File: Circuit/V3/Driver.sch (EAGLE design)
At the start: 36 parts

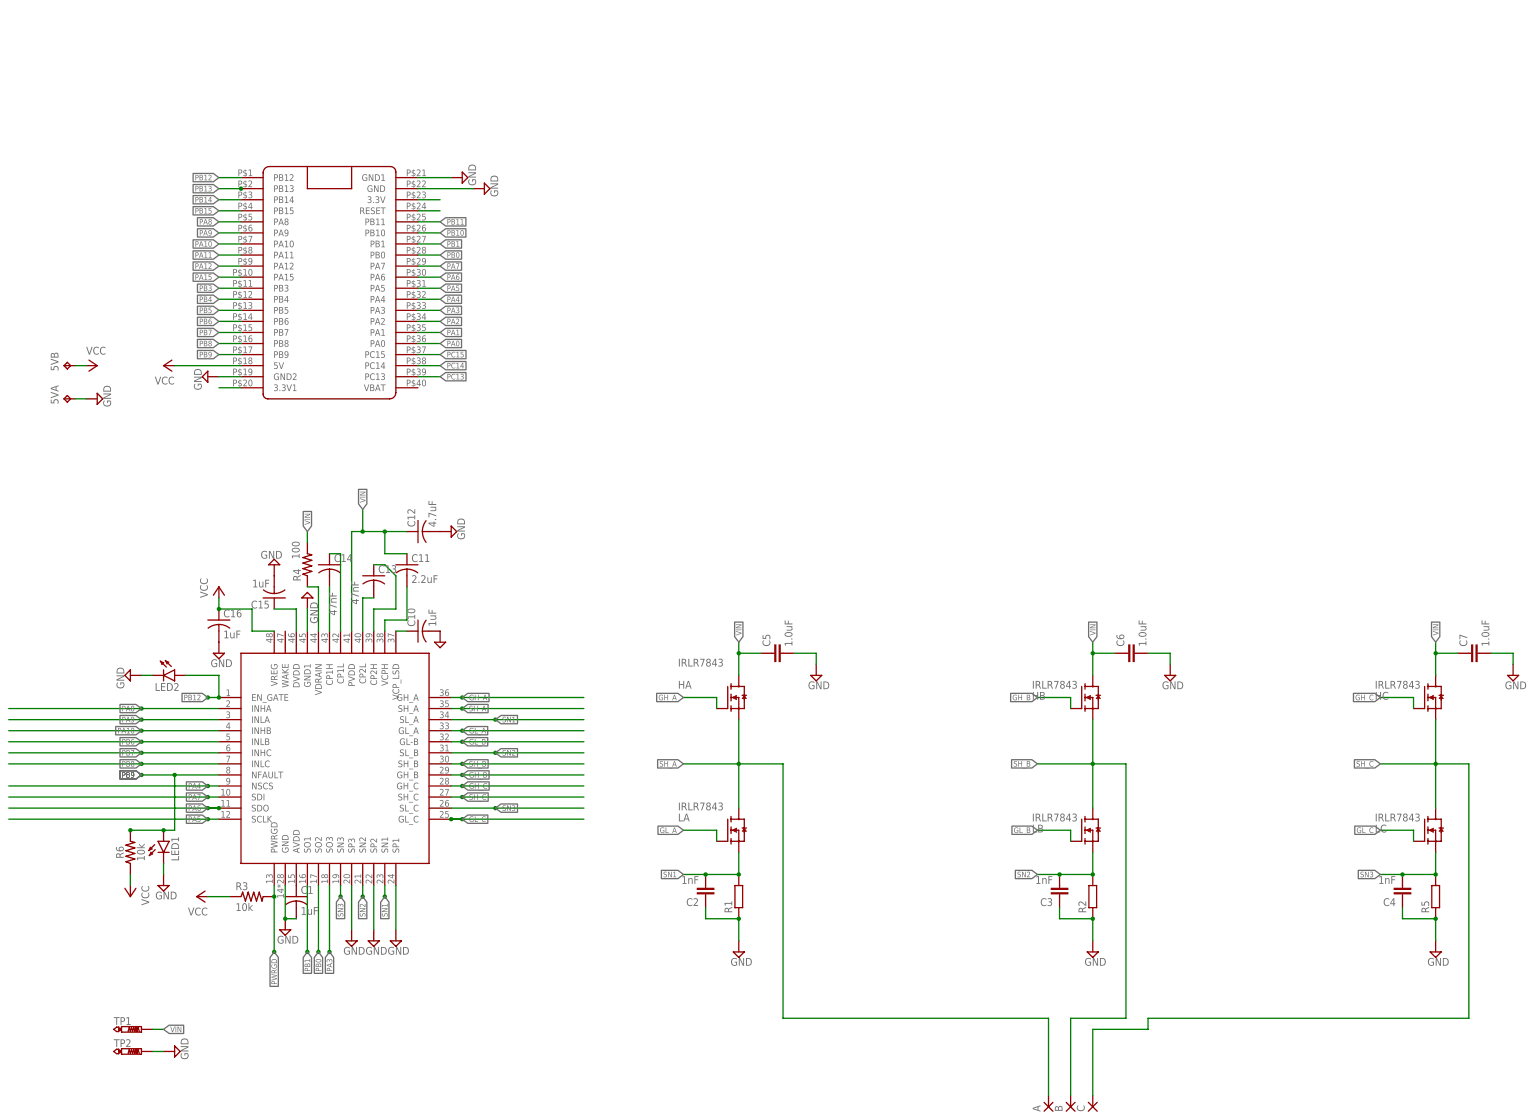
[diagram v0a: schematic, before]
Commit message: Change the orginal motor gate driver(DRV8305) to DRV8303 in schematic
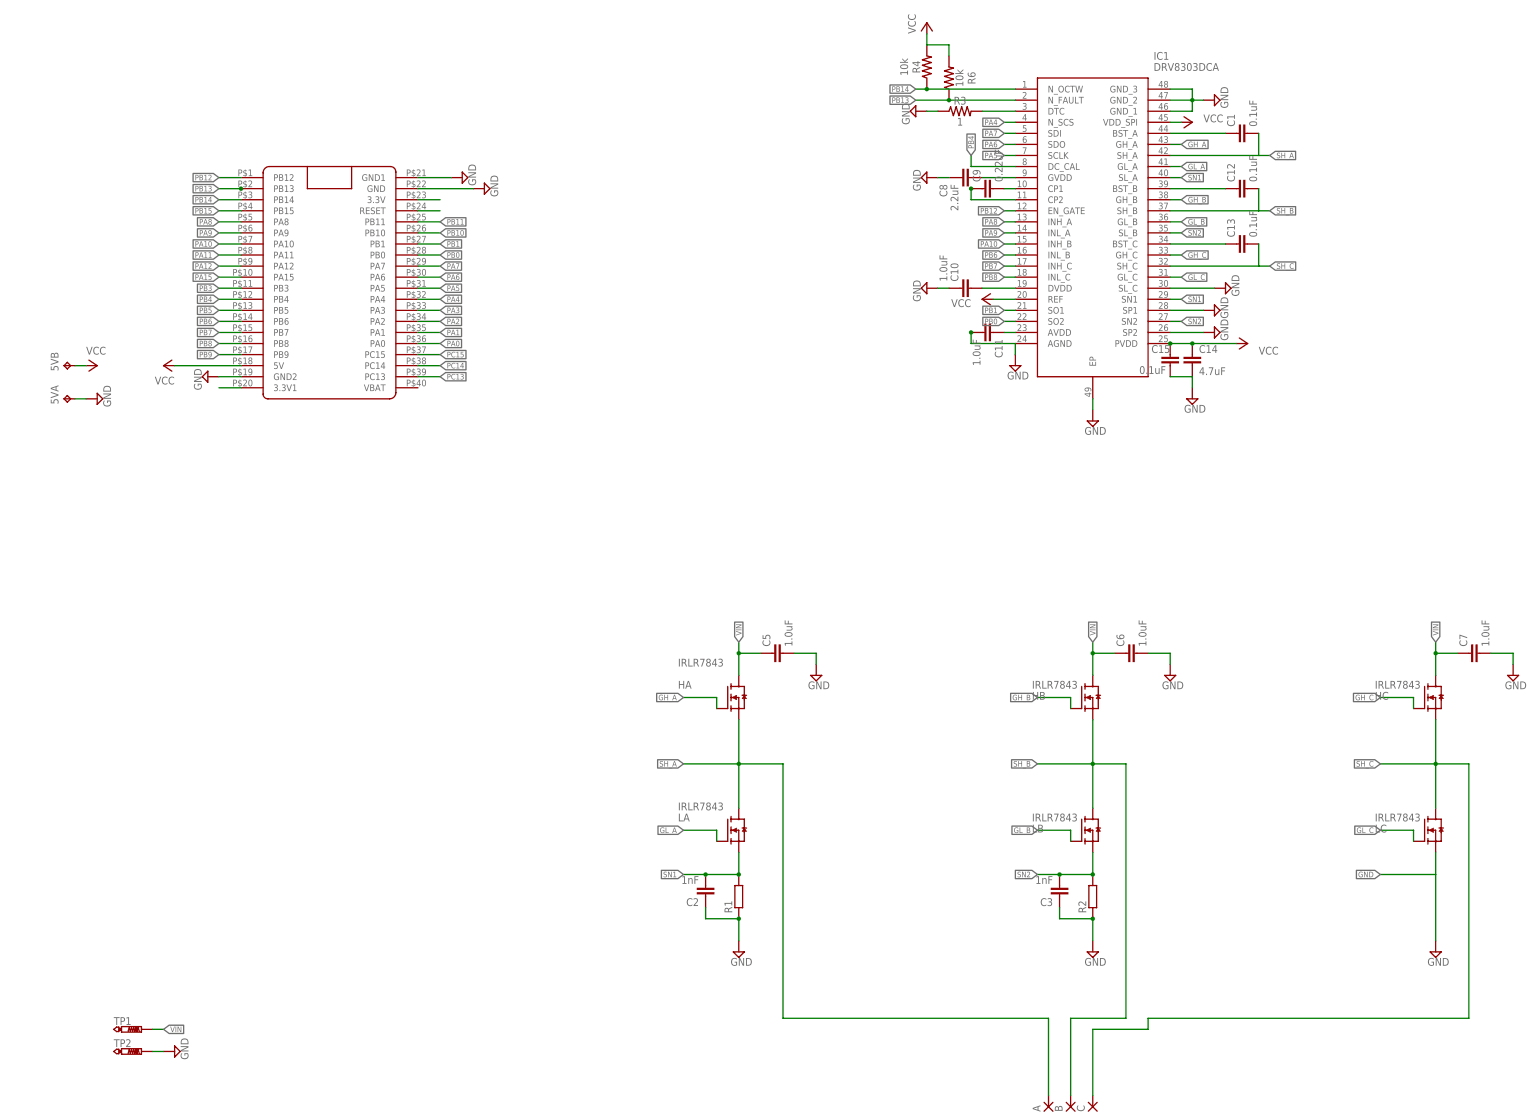
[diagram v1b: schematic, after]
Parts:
- removed C16: 1uF, rcl:C-USC0603
- removed C4: 1nF, SparkFun-Capacitors:1.0NF/1000PF-0603-50V-10%
- removed LED1, LED2: (no value), led:LEDCHIPLED_0805
- removed R5: (no value), rcl:R-EU_R2512
- removed U$3: DRV8305, BLDC project:DRV8305
- added C8: 2.2uF, SparkFun-Capacitors:2.2UF-0603-10V-20%
- added C9: 0.22uF, SparkFun-Capacitors:0.22UF-0603-25V-10%
- added IC1: DRV8303DCA, DRV8303DCA:DRV8303DCA
- C1, C15: value 1uF -> 0.1uF; device rcl:C-USC0603 -> SparkFun-Capacitors:0.1UF-0603-25V-(+80/-20%)
- C10: value 1uF -> 1.0uF; device rcl:C-USC0603 -> SparkFun-Capacitors:1.0UF-0603-16V-10%
- C11: value 2.2uF -> 1.0uF; device rcl:C-USC0603 -> SparkFun-Capacitors:1.0UF-0603-16V-10%
- C12: value 4.7uF -> 0.1uF; device rcl:C-USC0603 -> SparkFun-Capacitors:0.1UF-0603-25V-(+80/-20%)
- C13: value 47nF -> 0.1uF; device rcl:C-USC0603 -> SparkFun-Capacitors:0.1UF-0603-25V-(+80/-20%)
- C14: value 47nF -> 4.7uF; device rcl:C-USC0603 -> SparkFun-Capacitors:4.7UF-0603-35V-(20%)
- R3: value 10k -> 1; device rcl:R-US_R0603 -> SparkFun-Resistors:1OHM-0603-1/10W-1%
- R4: value 100 -> 10k; device rcl:R-US_R0603 -> SparkFun-Resistors:10KOHM-0603-1/10W-1%
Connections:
- removed net CP1H: C14.2, U$3.CP1H
- removed net CP1L: C14.1, U$3.CP1L
- removed net CP2H: C13.1, U$3.CP2H
- removed net CP2L: C13.2, U$3.CP2L
- removed net DVDD: C15.1, U$3.DVDD
- removed net N$15: C1.1, U$3.AVDD
- removed net PWRGD: R3.2, U$3.PWRGD
- removed net SN3: C4.2, LC.S, R5.2, U$3.SL_C, U$3.SN3
- removed net VCPH: C11.2, U$3.VCPH
- removed net VCP_LSD: C10.1, U$3.VCP_LSD
- removed net VDRAIN: R4.1, U$3.VDRAIN
- new net N$14: C13.1, IC1.BST_C
- new net N$2: C1.1, IC1.BST_A
- new net N$26: IC1.DTC, R3.2
- new net N$32: C8.1, IC1.GVDD
- new net N$33: C9.2, IC1.CP1
- new net N$34: C9.1, IC1.CP2
- new net N$43: C10.2, IC1.DVDD
- new net N$47: C11.1, IC1.AVDD
- new net N$9: C12.1, IC1.BST_B
- net GH_A: now also IC1.GH_A; no longer U$3.GH_A
- net GH_B: now also IC1.GH_B; no longer U$3.GH_B
- net GH_C: now also IC1.GH_C; no longer U$3.GH_C
- net GL_A: now also IC1.GL_A; no longer U$3.GL_A
- net GL_B: now also IC1.GL_B; no longer U$3.GL-B
- net GL_C: now also IC1.GL_C; no longer U$3.GL_C
- net GND: now also C10.1, C11.2, C14.2, C8.2, IC1.AGND, IC1.EP, IC1.GND_1, IC1.GND_2, IC1.GND_3, IC1.SL_C, IC1.SP1, IC1.SP2, LC.S, R3.1; no longer C1.2, C10.2, C12.2, C16.2, C4.1, LED1.C, LED2.C, R5.1, U$3.GND, U$3.GND1, U$3.SP1, U$3.SP2, U$3.SP3
- net PA10: now also IC1.INH_B; no longer U$3.INHB
- net PA3: no longer U$3.SO3
- net PA4: now also IC1.N_SCS; no longer U$3.NSCS
- net PA5: now also IC1.SCLK; no longer U$3.SCLK
- net PA6: now also IC1.SDO; no longer U$3.SDO
- net PA7: now also IC1.SDI; no longer U$3.SDI
- net PA8: now also IC1.INH_A; no longer U$3.INHA
- net PA9: now also IC1.INL_A; no longer U$3.INLA
- net PB0: now also IC1.SO2; no longer U$3.SO2
- net PB1: now also IC1.SO1; no longer U$3.SO1
- net PB12: now also IC1.EN_GATE; no longer LED2.A, U$3.EN_GATE
- net PB13: now also IC1.N_FAULT, R6.1
- net PB14: now also IC1.N_OCTW, R4.1
- net PB4: now also IC1.DC_CAL
- net PB6: now also IC1.INL_B; no longer U$3.INLB
- net PB7: now also IC1.INH_C; no longer U$3.INHC
- net PB8: now also IC1.INL_C; no longer U$3.INLC
- net PB9: no longer LED1.A, R6.2, U$3.NFAULT
- net SH_A: now also C1.2, IC1.SH_A; no longer U$3.SH_A
- net SH_B: now also C12.2, IC1.SH_B; no longer U$3.SH_B
- net SH_C: now also C13.2, IC1.SH_C; no longer U$3.SH_C
- net SN1: now also IC1.SL_A, IC1.SN1; no longer U$3.SL_A, U$3.SN1
- net SN2: now also IC1.SL_B, IC1.SN2; no longer U$3.SL_B, U$3.SN2
- net VCC: now also C14.1, C15.1, IC1.PVDD, IC1.REF, IC1.VDD_SPI, R4.2, R6.2; no longer C16.1, R3.1, R6.1, U$3.VREG
- net VIN: no longer C11.1, C12.1, R4.2, U$3.PVDD
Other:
- moved on the sheet: C1, C10, C11, C12, C13, C14, C15, R3, R4, R6

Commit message: Routing the basic circuit and route. A backup before autorouting
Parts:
- added D1, D2: BLUE, SparkFun-LED:LED-BLUE0603
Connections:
- net GND: now also D1.C, D2.C
- net PB12: now also D2.A
- net PB13: now also D1.A
- net VCC: no longer C14.1, C15.1, IC1.PVDD
- net VIN: now also C14.1, C15.1, IC1.PVDD
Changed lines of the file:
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@@
 <part name="SUPPLY17" library="supply2" library_urn="urn:adsk.eagle:library:372" deviceset="GND" device=""/>
 <part name="SUPPLY18" library="supply2" library_urn="urn:adsk.eagle:library:372" deviceset="GND" device=""/>
-<part name="P+6" library="supply1" library_urn="urn:adsk.eagle:library:371" deviceset="VCC" device=""/>
 <part name="C14" library="SparkFun-Capacitors" deviceset="4.7UF" device="-0603-35V-(20%)" value="4.7uF"/>
 <part name="C15" library="SparkFun-Capacitors" deviceset="0.1UF" device="-0603-25V-(+80/-20%)" value="0.1uF"/>
 <part name="SUPPLY19" library="supply2" library_urn="urn:adsk.eagle:library:372" deviceset="GND" device=""/>
 <part name="SUPPLY21" library="supply2" library_urn="urn:adsk.eagle:library:372" deviceset="GND" device=""/>
+<part name="D1" library="SparkFun-LED" deviceset="LED-BLUE" device="0603" value="BLUE"/>
+<part name="D2" library="SparkFun-LED" deviceset="LED-BLUE" device="0603" value="BLUE"/>
+<part name="SUPPLY22" library="supply2" library_urn="urn:adsk.eagle:library:372" deviceset="GND" device=""/>
+<part name="SUPPLY23" library="supply2" library_urn="urn:adsk.eagle:library:372" deviceset="GND" device=""/>
 </parts>
 <sheets>
@@
 <attribute name="VALUE" x="264.795" y="92.075" size="1.778" layer="96" rot="R90"/>
 </instance>
-<instance part="P+6" gate="VCC" x="269.24" y="91.44" smashed="yes" rot="R270">
-<attribute name="VALUE" x="271.78" y="88.9" size="1.778" layer="96"/>
-</instance>
 <instance part="C14" gate="G$1" x="256.54" y="86.36" smashed="yes">
 <attribute name="NAME" x="258.064" y="89.281" size="1.778" layer="95" font="vector"/>
@@
 <instance part="SUPPLY21" gate="GND" x="264.16" y="104.14" smashed="yes" rot="R90">
 <attribute name="VALUE" x="267.335" y="102.235" size="1.778" layer="96" rot="R90"/>
+</instance>
+<instance part="D1" gate="G$1" x="185.42" y="144.78" smashed="yes">
+<attribute name="NAME" x="181.991" y="140.208" size="1.778" layer="95" font="vector" rot="R90"/>
+<attribute name="VALUE" x="187.325" y="140.208" size="1.778" layer="96" font="vector" rot="R90" align="top-left"/>
+</instance>
+<instance part="D2" gate="G$1" x="198.12" y="119.38" smashed="yes">
+<attribute name="NAME" x="194.691" y="114.808" size="1.778" layer="95" font="vector" rot="R90"/>
+<attribute name="VALUE" x="200.025" y="114.808" size="1.778" layer="96" font="vector" rot="R90" align="top-left"/>
+</instance>
+<instance part="SUPPLY22" gate="GND" x="185.42" y="134.62" smashed="yes">
+<attribute name="VALUE" x="183.515" y="131.445" size="1.778" layer="96"/>
+</instance>
+<instance part="SUPPLY23" gate="GND" x="193.04" y="114.3" smashed="yes" rot="R270">
+<attribute name="VALUE" x="189.865" y="116.205" size="1.778" layer="96" rot="R270"/>
 </instance>
 </instances>
@@
 <pinref part="SUPPLY21" gate="GND" pin="GND"/>
 </segment>
+<segment>
+<pinref part="D1" gate="G$1" pin="C"/>
+<wire x1="185.42" y1="139.7" x2="185.42" y2="137.16" width="0.1524" layer="91"/>
+<pinref part="SUPPLY22" gate="GND" pin="GND"/>
+</segment>
+<segment>
+<pinref part="D2" gate="G$1" pin="C"/>
+<wire x1="198.12" y1="114.3" x2="195.58" y2="114.3" width="0.1524" layer="91"/>
+<pinref part="SUPPLY23" gate="GND" pin="GND"/>
+</segment>
 </net>
 <net name="N$3" class="0">
@@
 <pinref part="TP1" gate="G$1" pin="TP"/>
 </segment>
+<segment>
+<pinref part="IC1" gate="G$1" pin="PVDD"/>
+<wire x1="251.46" y1="91.44" x2="256.54" y2="91.44" width="0.1524" layer="91"/>
+<pinref part="C14" gate="G$1" pin="1"/>
+<wire x1="256.54" y1="91.44" x2="266.7" y2="91.44" width="0.1524" layer="91"/>
+<junction x="256.54" y="91.44"/>
+<pinref part="C15" gate="G$1" pin="1"/>
+<junction x="251.46" y="91.44"/>
+<label x="266.7" y="91.44" size="1.778" layer="95" xref="yes"/>
+</segment>
 </net>
 <net name="PB12" class="0">
@@
 <segment>
 <pinref part="IC1" gate="G$1" pin="EN_GATE"/>
-<wire x1="215.9" y1="121.92" x2="213.36" y2="121.92" width="0.1524" layer="91"/>
-<label x="213.36" y="121.92" size="1.27" layer="95" rot="R180" xref="yes"/>
+<wire x1="215.9" y1="121.92" x2="198.12" y2="121.92" width="0.1524" layer="91"/>
+<label x="195.58" y="121.92" size="1.27" layer="95" rot="R180" xref="yes"/>
+<pinref part="D2" gate="G$1" pin="A"/>
+<wire x1="198.12" y1="121.92" x2="195.58" y2="121.92" width="0.1524" layer="91"/>
+<junction x="198.12" y="121.92"/>
 </segment>
 </net>
@@
 <pinref part="IC1" gate="G$1" pin="N_FAULT"/>
 <wire x1="215.9" y1="147.32" x2="200.66" y2="147.32" width="0.1524" layer="91"/>
-<label x="193.04" y="147.32" size="1.27" layer="95" rot="R180" xref="yes"/>
+<label x="182.88" y="147.32" size="1.27" layer="95" rot="R180" xref="yes"/>
 <pinref part="R6" gate="G$1" pin="1"/>
-<wire x1="200.66" y1="147.32" x2="193.04" y2="147.32" width="0.1524" layer="91"/>
+<wire x1="200.66" y1="147.32" x2="185.42" y2="147.32" width="0.1524" layer="91"/>
 <junction x="200.66" y="147.32"/>
+<pinref part="D1" gate="G$1" pin="A"/>
+<wire x1="185.42" y1="147.32" x2="182.88" y2="147.32" width="0.1524" layer="91"/>
+<junction x="185.42" y="147.32"/>
 </segment>
 </net>
@@
 <pinref part="P+4" gate="VCC" pin="VCC"/>
 </segment>
-<segment>
-<pinref part="IC1" gate="G$1" pin="PVDD"/>
-<wire x1="251.46" y1="91.44" x2="256.54" y2="91.44" width="0.1524" layer="91"/>
-<pinref part="P+6" gate="VCC" pin="VCC"/>
-<pinref part="C14" gate="G$1" pin="1"/>
-<wire x1="256.54" y1="91.44" x2="266.7" y2="91.44" width="0.1524" layer="91"/>
-<junction x="256.54" y="91.44"/>
-<pinref part="C15" gate="G$1" pin="1"/>
-<junction x="251.46" y="91.44"/>
-</segment>
-</net>
+</net>
